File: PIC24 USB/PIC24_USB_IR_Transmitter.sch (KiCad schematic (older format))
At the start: 24 parts, among them CON1 USB-MINI-B, P1 CONN_6, P2 CONN_4, P3 CONN_6, P4 CONN_6, P5 CONN_4, P6 CONN_1, P7 CONN_8, P8 CONN_8X2, Q1 2N7002, U2 LM1117_SOT223_3V3

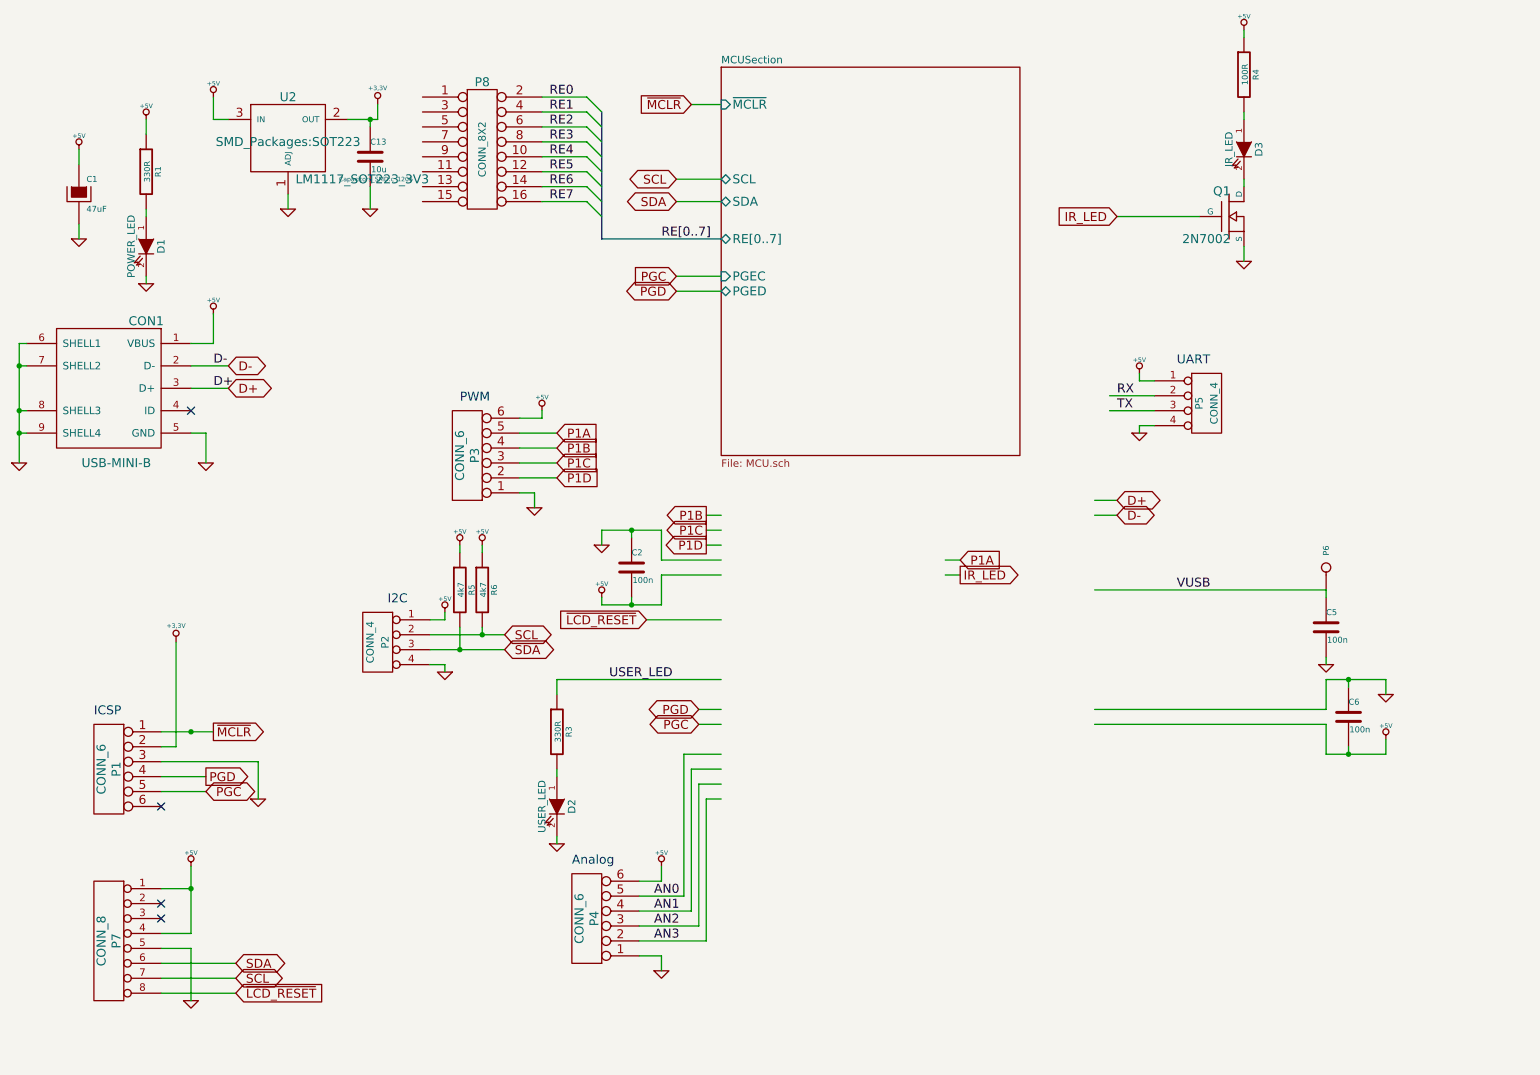
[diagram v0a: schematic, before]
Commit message: added led display, many additional headers and DAC
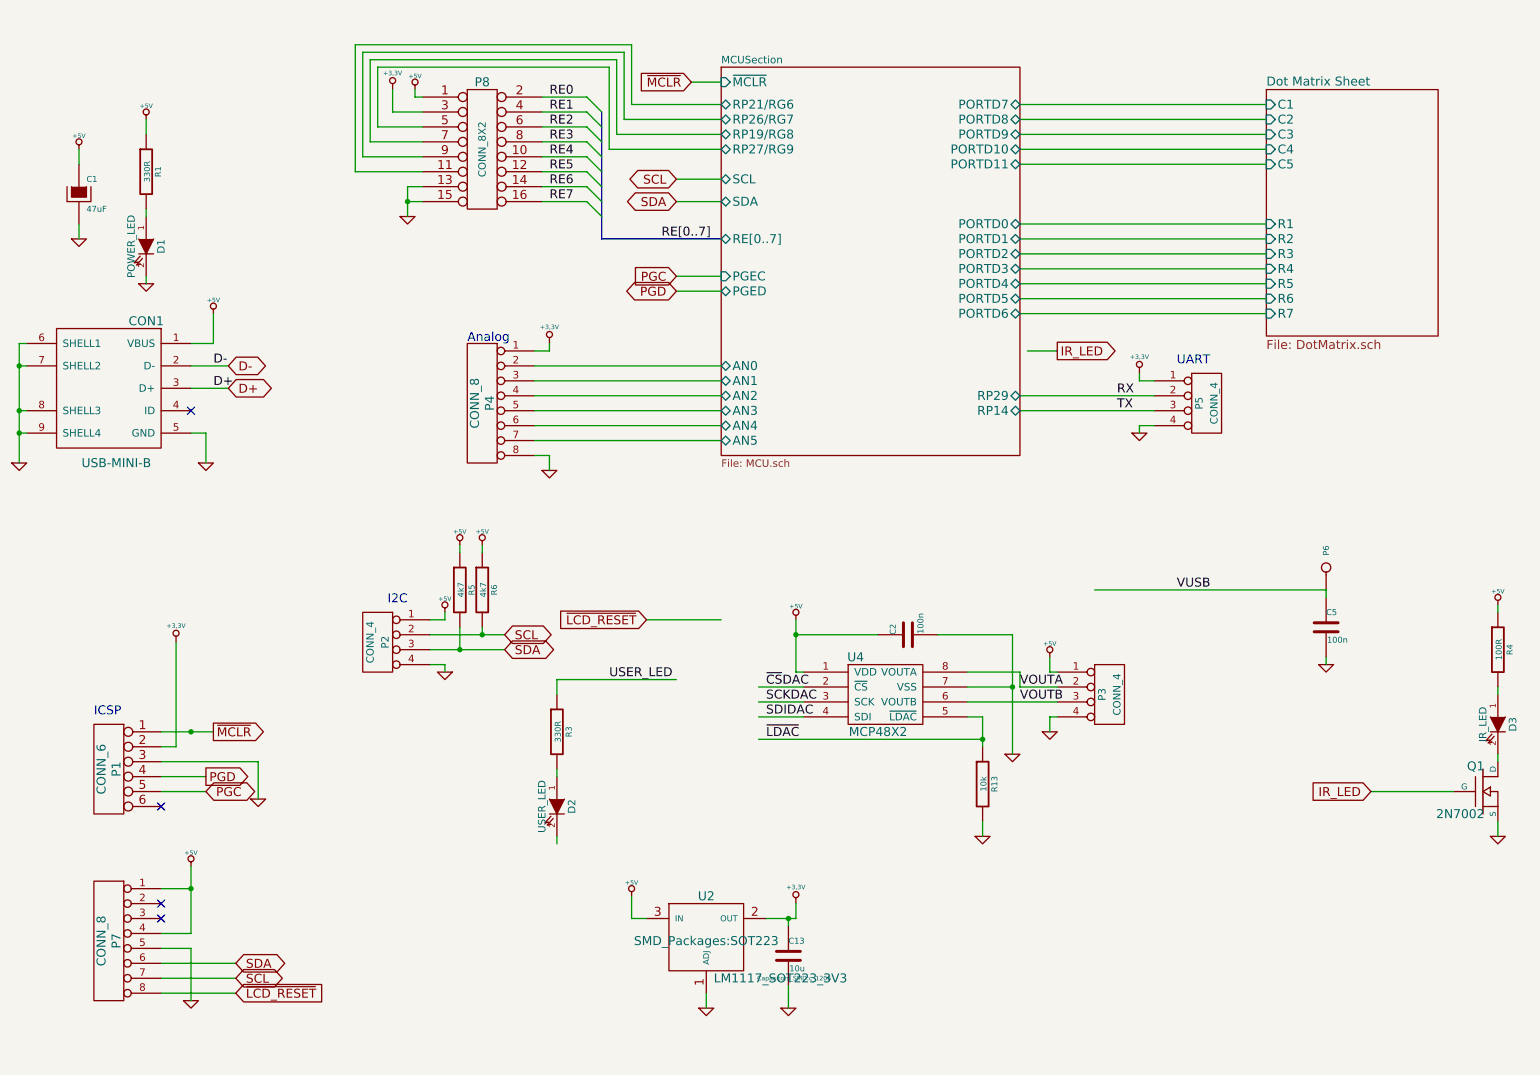
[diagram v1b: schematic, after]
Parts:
- removed C6: 100n, Capacitors_SMD:c_0603, symbol C
- removed P3, P4: CONN_6, Pin_Headers:Pin_Header_Straight_1x06, symbol CONN_6
- added P3: CONN_4, Pin_Headers:Pin_Header_Straight_1x04, symbol CONN_4
- added P4: CONN_8, Pin_Headers:Pin_Header_Straight_1x08, symbol CONN_8
- added R13: 10k, SMD_Packages:SMD-0603_r, symbol R
- added U4: MCP48X2, SMD_Packages:MSOP-8, symbol MCP48X2
- C1: footprint c_tant_B -> Capacitors_Tantalum_SMD:TantalC_SizeB_EIA-3528_HandSoldering
- C2, C5: footprint Capacitors_SMD:c_0603 -> SMD_Packages:SMD-0603_c
- P1: footprint Connect:PINHEAD1-6 -> Pin_Headers:Pin_Header_Angled_1x06
- Q1: footprint Transistors_SMD:sot23 -> SMD_Packages:SOT-23-GDS
- R1, R3, R5, R6: footprint SMD_Packages:SM0603_Resistor -> SMD_Packages:SMD-0603_r
- R4: footprint SMD_Packages:SM1206 -> SMD_Packages:SMD-1206
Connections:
- net labels added: SCKDAC, SDIDAC, VOUTA, VOUTB, ~CS~DAC, ~LDAC~
- net labels removed: AN0, AN1, AN2, AN3, P1A, P1B, P1C, P1D
- wire segments 133 -> 151
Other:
- note removed: "PWM"
- moved on the sheet: C13, C2, D3, Q1, R4, U2

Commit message: more hierarchical pin for MCU section, connected USB lines in schematic
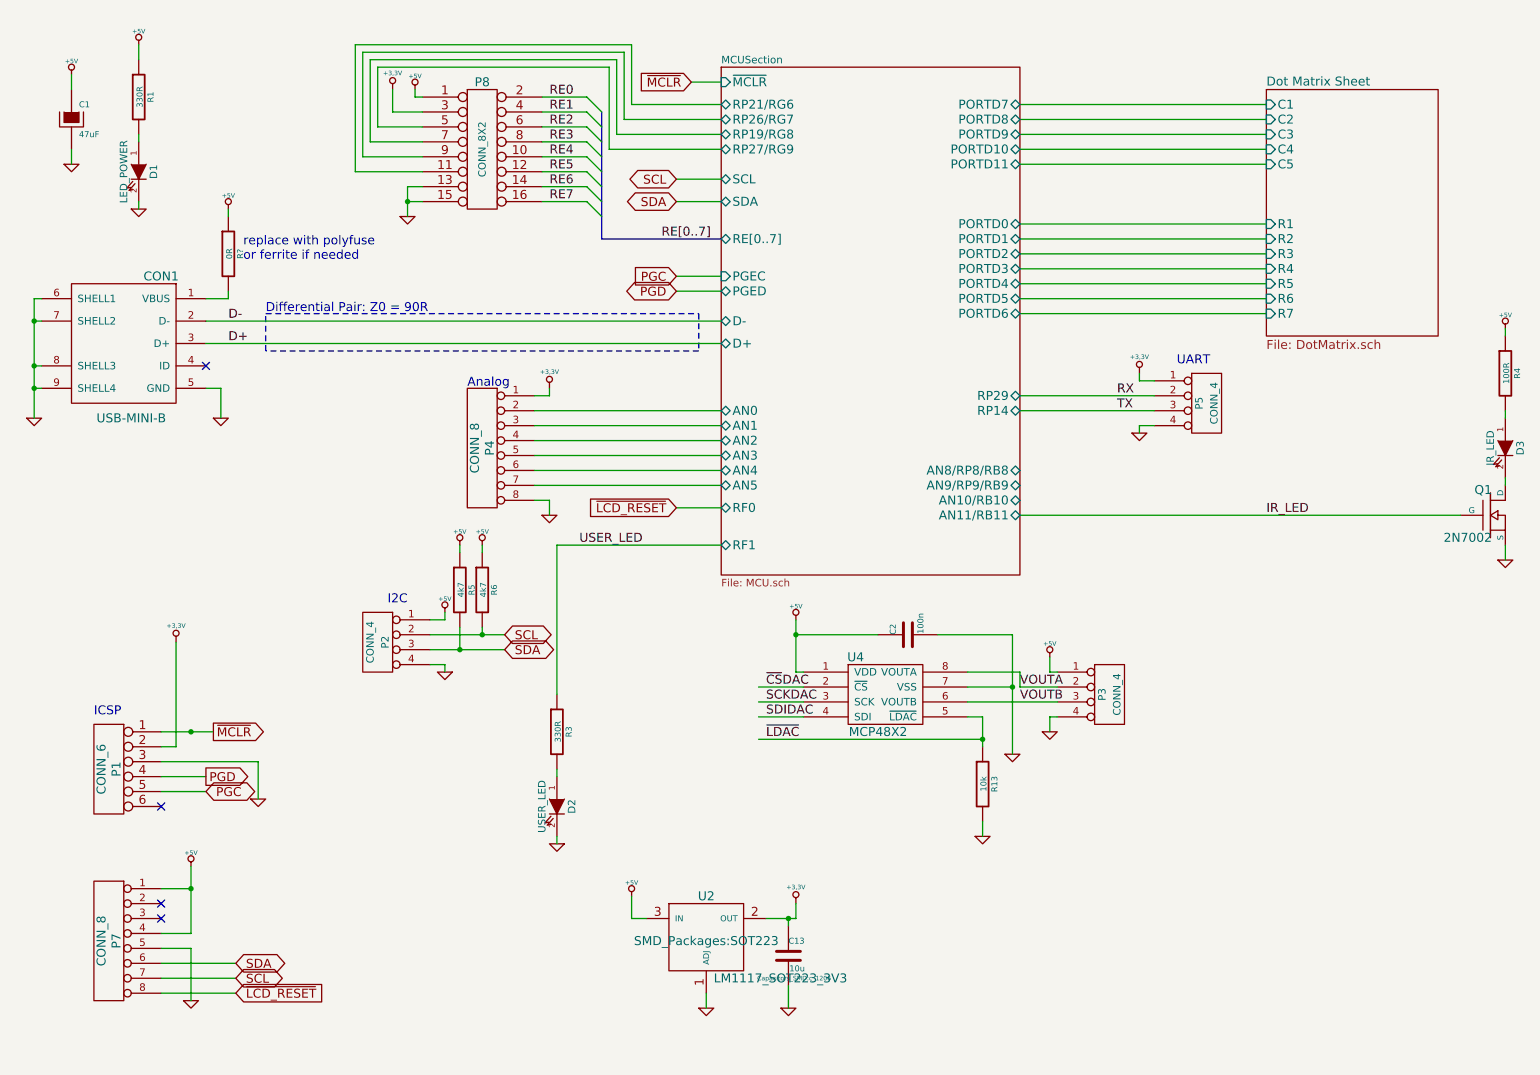
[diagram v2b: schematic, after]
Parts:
- removed C5: 100n, SMD_Packages:SMD-0603_c, symbol C
- removed P6: CONN_1, Pin_Headers:Pin_Header_Straight_1x01, symbol CONN_1
- added R?: 0R, symbol R
- D1: value POWER_LED -> LED_POWER
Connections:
- net labels removed: VUSB
- wire segments 151 -> 148
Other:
- note added: "Differential Pair: Z0 = 90R\n"
- note added: "replace with polyfuse\nor ferrite if needed"
- moved on the sheet: C1, CON1, D1, D3, P4, Q1, R1, R4

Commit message: connected SPI DAC
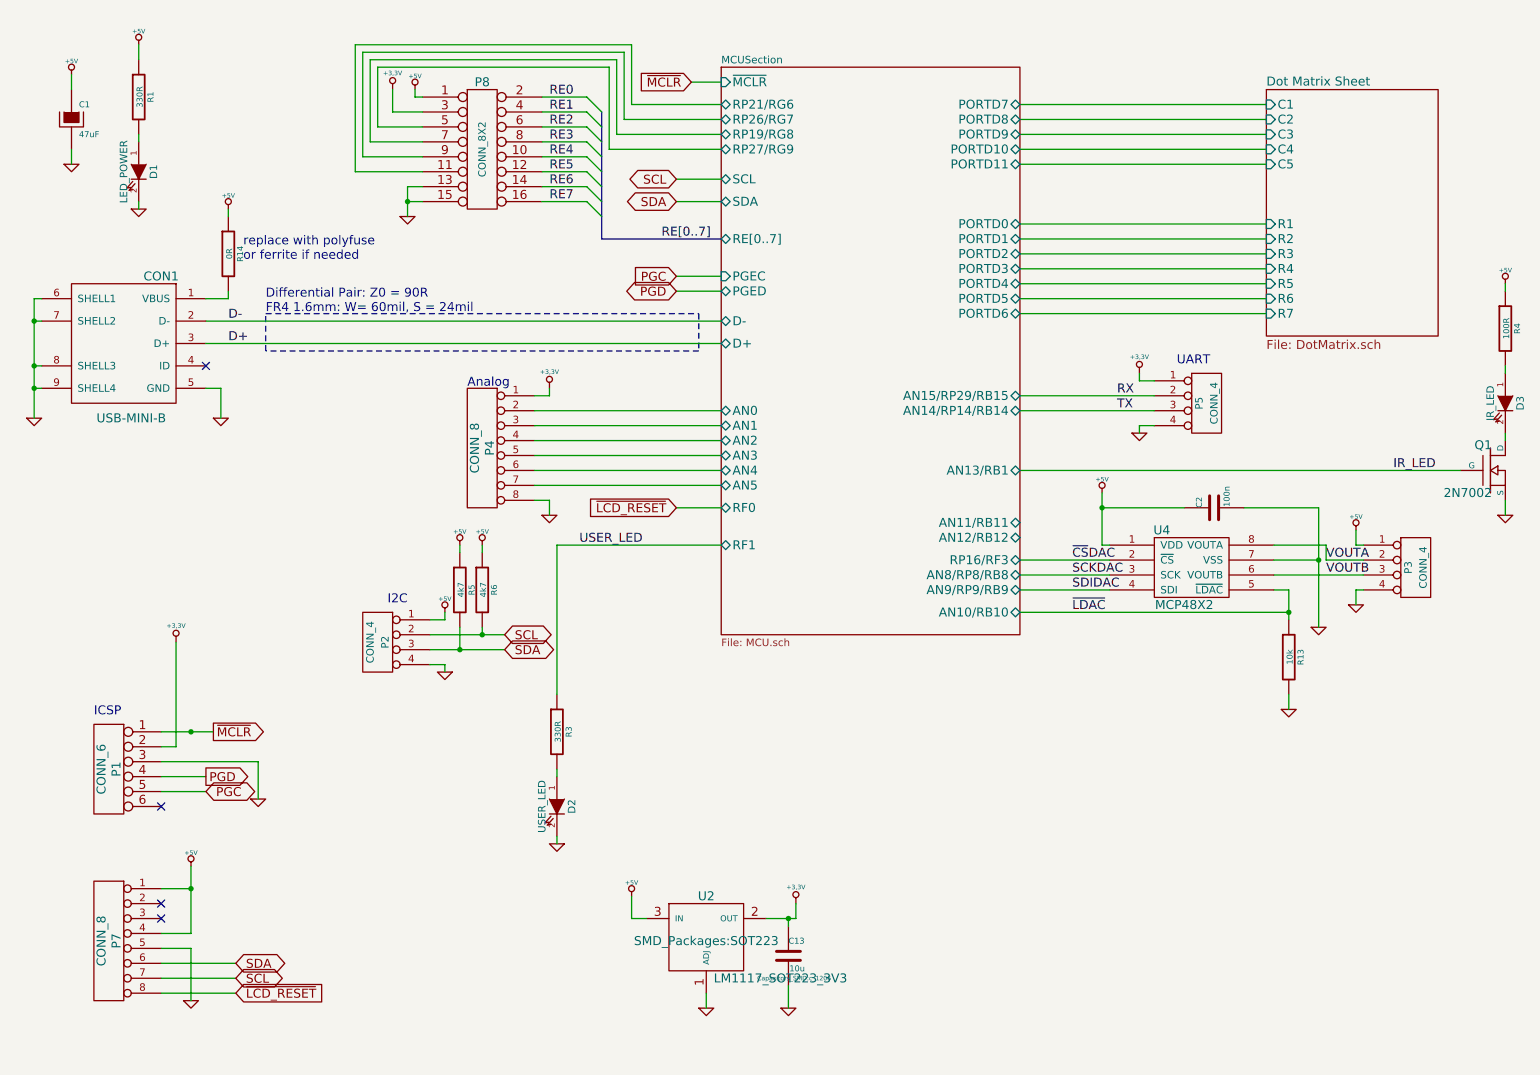
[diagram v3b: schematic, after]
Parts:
- gave numbers to parts that had none: 1
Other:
- note added: "Differential Pair: Z0 = 90R\nFR4 1.6mm: W= 60mil, S = 24mil\n"
- note removed: "Differential Pair: Z0 = 90R\n"
- moved on the sheet: C2, D3, P3, Q1, R13, R4, U4

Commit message: done a lot of work: ready for submission
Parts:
- added P6: CONN_1, Symbols:Symbol_OSHW-Logo_CopperTop, symbol CONN_1
- R14: footprint (none) -> SMD_Packages:SMD-1206
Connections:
- net +3.3V: now also P1.5; no longer P1.2
- net GND: now also P1.4; no longer P1.3
- net PGC: now also P1.2; no longer P1.5
- net PGD: now also P1.3; no longer P1.4
- net ~MCLR~: now also P1.6; no longer P1.1
- net VIN: now reaches CON1.1 (VBUS), R14.2
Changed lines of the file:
@@
 Comment4 ""
 $EndDescr
-$Comp
-L USB-MINI-B CON1
-U 1 1 52D43B15
-P 1550 2850
-F 0 "CON1" H 1300 3300 60  0000 C CNN
-F 1 "USB-MINI-B" H 1500 2350 60  0000 C CNN
-F 2 "Connect:USB_MINI_B" H 1550 2850 60  0001 C CNN
-F 3 "" H 1550 2850 60  0000 C CNN
-	1    1550 2850
-	-1   0    0    -1
-$EndComp
 Wire Wire Line
 	950  2550 950  3350
@@
 F 3 "" H 1450 5700 60  0000 C CNN
 	1    1450 5700
-	-1   0    0    -1
+	-1   0    0    1
 $EndComp
 Text Notes 1350 5350 0    60   ~ 0
@@
 F 0 "R14" V 2330 2250 40  0000 C CNN
 F 1 "0R" V 2257 2251 40  0000 C CNN
-F 2 "" V 2180 2250 30  0000 C CNN
+F 2 "SMD_Packages:SMD-1206" V 2180 2250 30  0001 C CNN
 F 3 "" H 2250 2250 30  0000 C CNN
 	1    2250 2250
@@
 F32 "RF0" B L 5550 3950 60
 F33 "RF1" B L 5550 4200 60
-F34 "AN8/RP8/RB8" B R 7550 4400 60
-F35 "AN9/RP9/RB9" B R 7550 4500 60
+F34 "AN8/RP8/RB8" B R 7550 4500 60
+F35 "AN9/RP9/RB9" B R 7550 4400 60
 F36 "AN10/RB10" B R 7550 4650 60
 F37 "AN11/RB11" B R 7550 4050 60
@@
 F42 "RP16/RF3" B R 7550 4300 60
 $EndSheet
+$Comp
+L CONN_1 P6
+U 1 1 53EB4765
+P 7450 5500
+F 0 "P6" H 7530 5500 40  0000 L CNN
+F 1 "CONN_1" H 7450 5555 30  0001 C CNN
+F 2 "Symbols:Symbol_OSHW-Logo_CopperTop" H 7450 5500 60  0001 C CNN
+F 3 "" H 7450 5500 60  0000 C CNN
+	1    7450 5500
+	1    0    0    -1
+$EndComp
+Text Label 2100 2550 0    60   ~ 0
+VIN
+$Comp
+L USB-MINI-B CON1
+U 1 1 53ED0E9A
+P 1550 2850
+F 0 "CON1" H 1300 3300 60  0000 C CNN
+F 1 "USB-MINI-B" H 1500 2350 60  0000 C CNN
+F 2 "Connect:USB_MINI_B" H 1550 2850 60  0001 C CNN
+F 3 "" H 1550 2850 60  0000 C CNN
+	1    1550 2850
+	-1   0    0    -1
+$EndComp
 $EndSCHEMATC
